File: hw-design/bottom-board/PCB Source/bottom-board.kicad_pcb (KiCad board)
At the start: 2 copper layers, 172 x 140.5 mm, 330 parts, among them J1 Power Jack, J10 NYS215, J11 USB_B, J12 USB_A, J13 DIN_5, J14 DIN_5, J15 RJHSE-5381, J16 NYS215, J17 NYS215, J18 MJ-3536N, J2 HMI_POWER, J3 CB Adapter, J4 CB Adapter, J5 HMI_DATA, J6 SERIAL_DEBUG, J7 NYS215, J8 NYS215, J9 NYS215, K1 G6S-2, K2 G6S-2, Q1 2N7002, Q10 J110, Q11 J110, Q12 2N7002, Q13 2N7002, Q14 J110, Q15 J110, Q16 2N7002, Q17 J110, Q2 2N7002, Q3 2N7002, Q4 2N7002, Q5 BSS84, Q6 BSS84, Q8 J110, Q9 2N7002, U1 MURATA 5V, U10 LM358, U11 OPA1678, U12 OPA1678, U13 DG9426E, U14 LM4811, U16 RT9742, U17 6N136S, U18 ISL83086E, U2 LD1117S50TR_SOT223, U20 ADC122S021, U21 MIC2076A, U22 74LVC3G17, U24 MCP4922-EP, U3 AP2120N-3.3, U4 LD1117S50TR_SOT223, U5 AP2120N-3.3, U6 CS4265, U7 AT24CS08, U8 LM4562, U9 DG9426E, X1 24.576MHz

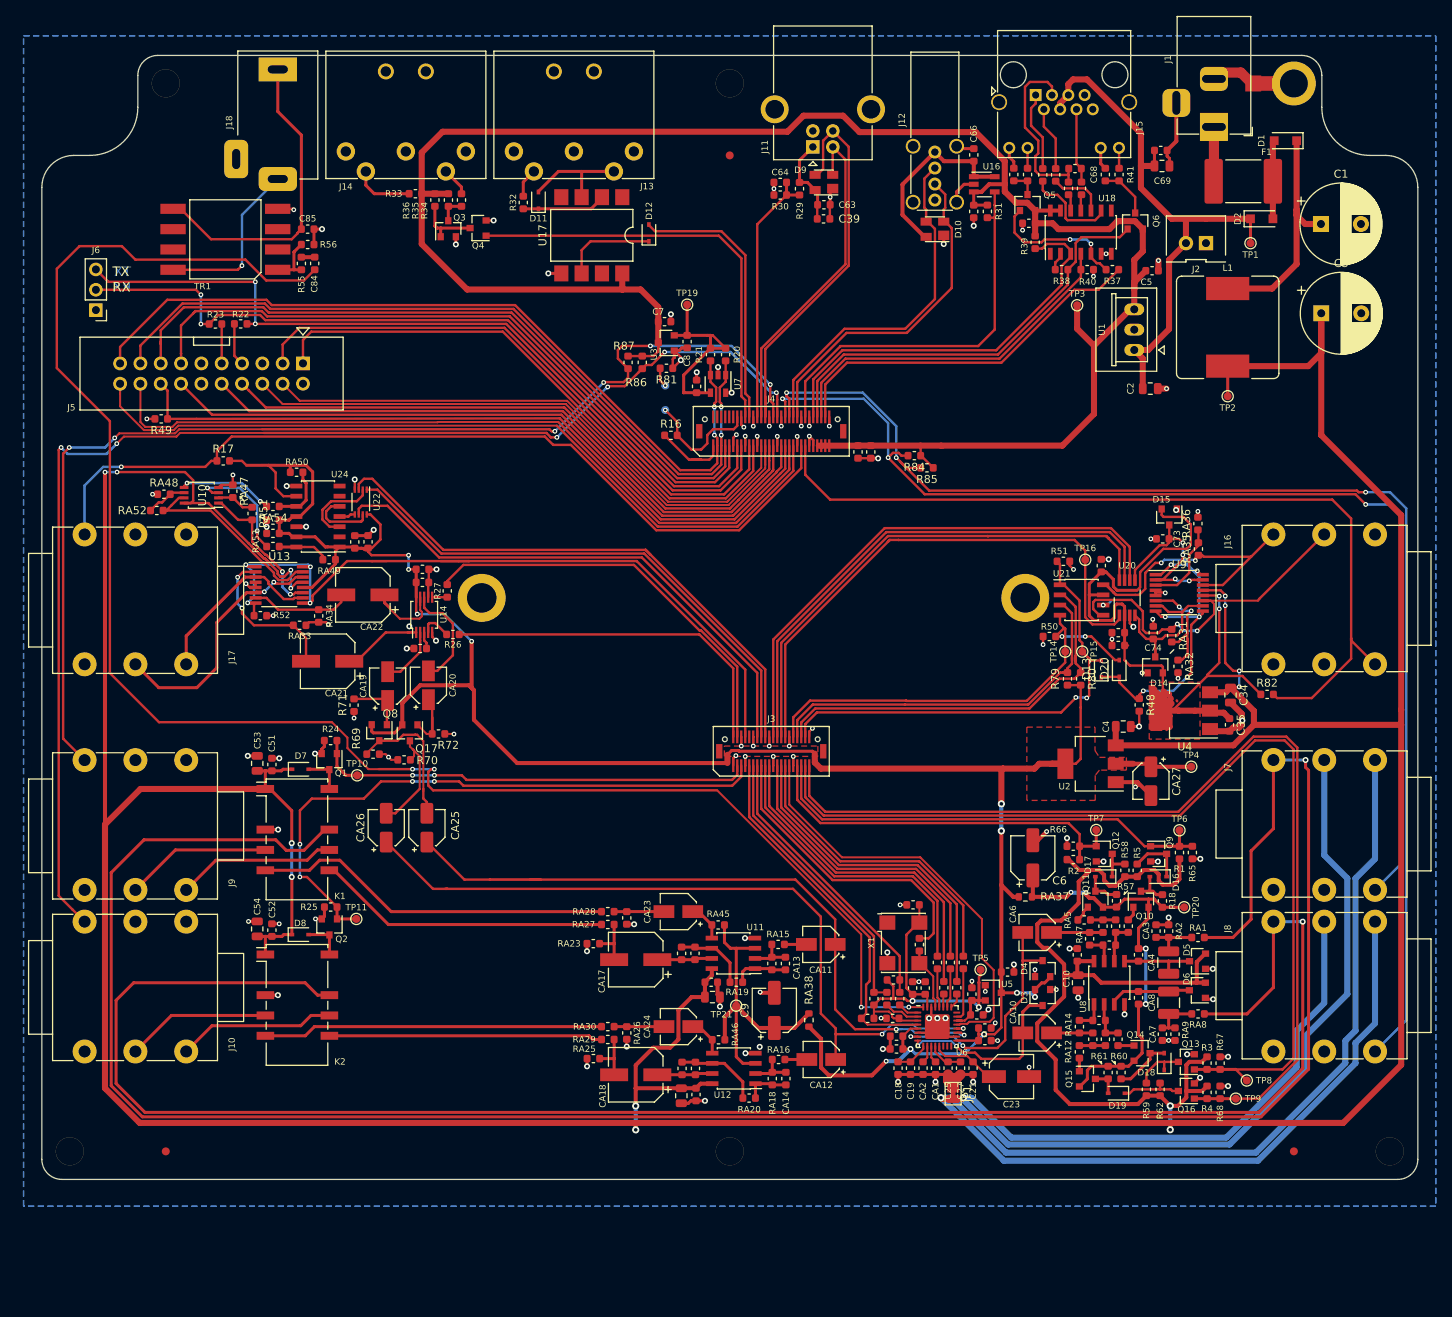
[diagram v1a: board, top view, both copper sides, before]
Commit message: route new output circuit
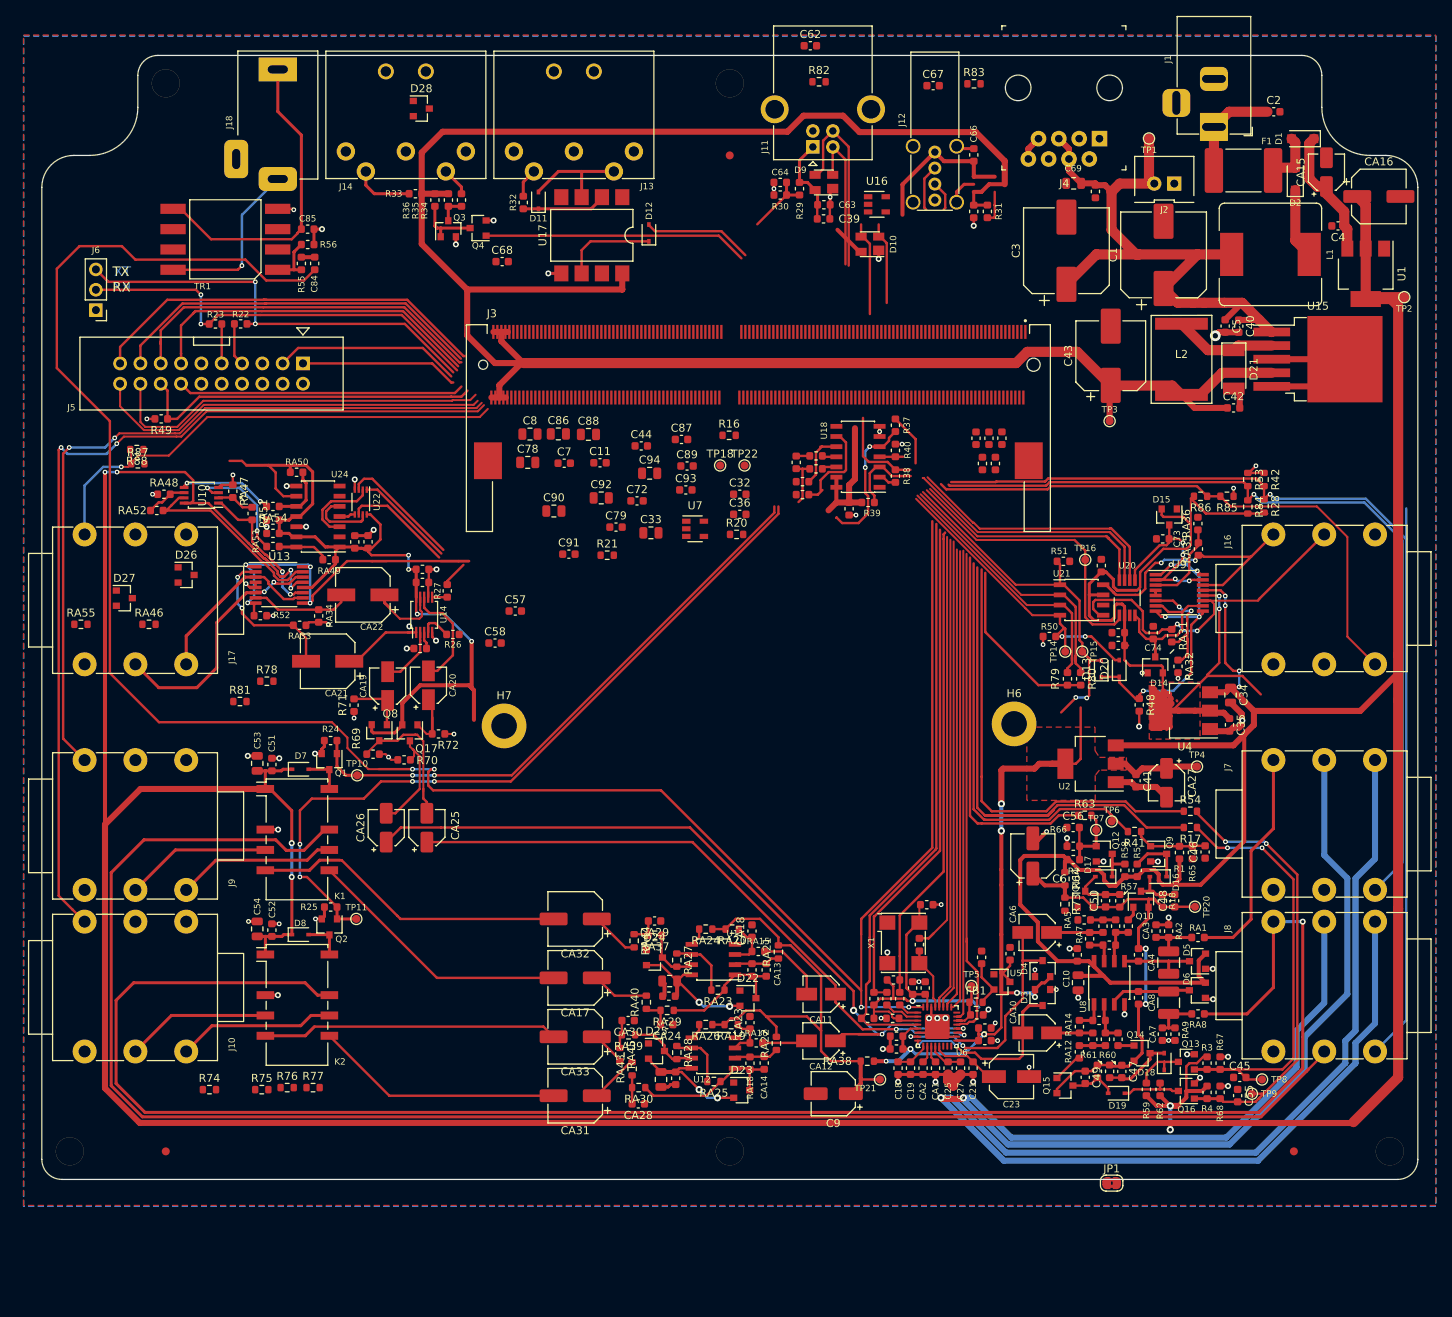
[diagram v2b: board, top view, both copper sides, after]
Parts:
- removed J15: RJHSE-5381, Connector_RJ:RJ45_Amphenol_RJHSE538X
- removed JMP1: 0R, footprints:Jumper_SMD_THT
- removed Q5, Q6: BSS84, Package_TO_SOT_SMD:SOT-23
- removed TP19: TestPoint, TestPoint:TestPoint_Pad_D1.0mm
- removed U3: AP2120N-3.3, Package_TO_SOT_SMD:SOT-23
- added C11: 100nF, Capacitor_SMD:C_0603_1608Metric, F.Cu at (129.8, 70.5)
- added C40: 100nF, Capacitor_SMD:C_0603_1608Metric, F.Cu at (209.7, 53.4)
- added C41: 100nF, Capacitor_SMD:C_0603_1608Metric, F.Cu at (196.8, 110.2)
- added C42: 100nF, Capacitor_SMD:C_0603_1608Metric, F.Cu at (209.0, 63.6)
- added C43: 470uF, Capacitor_SMD:CP_Elec_8x10.5, F.Cu at (193.7, 57.1)
- added C44: 1nF, Capacitor_SMD:C_0603_1608Metric, F.Cu at (135.0, 68.4)
- added C45: 100nF, Capacitor_SMD:C_0603_1608Metric, F.Cu at (209.8, 147.3)
- added C46: 100nF, Capacitor_SMD:C_0603_1608Metric, F.Cu at (205.5, 119.1)
- added C47: 100nF, Capacitor_SMD:C_0603_1608Metric, F.Cu at (195.1, 146.6)
- added C48: 100nF, Capacitor_SMD:C_0603_1608Metric, F.Cu at (201.7, 125.2)
- added C49: 100nF, Capacitor_SMD:C_0603_1608Metric, F.Cu at (190.5, 147.3)
- added C50: 100nF, Capacitor_SMD:C_0603_1608Metric, F.Cu at (193.0, 125.2)
- added C55: 100nF, Capacitor_SMD:C_0603_1608Metric, F.Cu at (209.6, 149.6)
- added C56: 100nF, Capacitor_SMD:C_0603_1608Metric, F.Cu at (189.0, 116.1)
- added C57: 100nF, Capacitor_SMD:C_0603_1608Metric, F.Cu at (119.3, 89.0)
- added C58: 100nF, Capacitor_SMD:C_0603_1608Metric, F.Cu at (116.7, 93.0)
- added C62: 1uF, Capacitor_SMD:C_0603_1608Metric, F.Cu at (156.1, 18.4)
- added C72: 100nF, Capacitor_SMD:C_0603_1608Metric, F.Cu at (134.5, 75.2)
- added C78: 22uF, Capacitor_SMD:C_0805_2012Metric, F.Cu at (120.8, 70.4)
- added C79: 100nF, Capacitor_SMD:C_0603_1608Metric, F.Cu at (131.8, 78.5)
- added C86: 22uF, Capacitor_SMD:C_0805_2012Metric, F.Cu at (124.6, 66.9)
- added C87: 100nF, Capacitor_SMD:C_0603_1608Metric, F.Cu at (140.0, 67.6)
- added C88: 22uF, Capacitor_SMD:C_0805_2012Metric, F.Cu at (128.4, 66.9)
- added C89: 100nF, Capacitor_SMD:C_0603_1608Metric, F.Cu at (140.7, 70.9)
- added C90: 22uF, Capacitor_SMD:C_0805_2012Metric, F.Cu at (124.1, 76.5)
- added C91: 100nF, Capacitor_SMD:C_0603_1608Metric, F.Cu at (126.0, 81.9)
- added C92: 22uF, Capacitor_SMD:C_0805_2012Metric, F.Cu at (130.0, 74.9)
- added C93: 100nF, Capacitor_SMD:C_0603_1608Metric, F.Cu at (140.6, 73.9)
- added C94: 22uF, Capacitor_SMD:C_0805_2012Metric, F.Cu at (136.1, 71.8)
- added CA28: 100pF, Capacitor_SMD:C_0603_1608Metric, F.Cu at (134.6, 150.6)
- added CA29: 100pF, Capacitor_SMD:C_0603_1608Metric, F.Cu at (136.7, 127.8)
- added CA30: 100pF, Capacitor_SMD:C_0603_1608Metric, F.Cu at (133.4, 140.2)
- added CA31: 47uF, Capacitor_SMD:CP_Elec_6.3x7.7, F.Cu at (126.7, 149.6)
- added CA32: 47uF, Capacitor_SMD:CP_Elec_6.3x7.7, F.Cu at (126.7, 127.5)
- added CA33: 47uF, Capacitor_SMD:CP_Elec_6.3x7.7, F.Cu at (126.7, 142.2)
- added D21: D_Schottky-Device, Diode_SMD:D_MELF, F.Cu at (209.1, 58.8)
- added D22: BAT54S, Package_TO_SOT_SMD:SOT-23, F.Cu at (148.3, 137.4)
- added D23: BAT54S, Package_TO_SOT_SMD:SOT-23, F.Cu at (147.6, 148.9)
- added D24: BAT54S, Package_TO_SOT_SMD:SOT-23, F.Cu at (136.7, 132.3)
- added D25: BAT54S, Package_TO_SOT_SMD:SOT-23, F.Cu at (136.9, 144.0)
- added D26: BAT54S, Package_TO_SOT_SMD:SOT-23, F.Cu at (78.1, 84.5)
- added D27: BAT54S, Package_TO_SOT_SMD:SOT-23, F.Cu at (70.4, 87.4)
- added D28: BAT54S, Package_TO_SOT_SMD:SOT-23, F.Cu at (107.5, 26.2)
- added FB1: Ferrite_Bead, Resistor_SMD:R_0603_1608Metric, F.Cu at (176.8, 137.9)
- added L2: 47UH 2A 135 MOHM, Uno:SRN8040TA, F.Cu at (202.5, 58.2)
- added R28: 100K, Resistor_SMD:R_0603_1608Metric, F.Cu at (212.9, 75.9)
- added R53: 56K, Resistor_SMD:R_0603_1608Metric, F.Cu at (210.8, 72.6)
- added R54: 1K, Resistor_SMD:R_0603_1608Metric, F.Cu at (203.6, 114.0)
- added R63: 1K, Resistor_SMD:R_0603_1608Metric, F.Cu at (190.4, 114.6)
- added R64: 1K, Resistor_SMD:R_0603_1608Metric, F.Cu at (188.0, 122.5)
- added R73: 1K5, Resistor_SMD:R_0603_1608Metric, F.Cu at (188.0, 125.7)
- added R74: 100K, Resistor_SMD:R_0603_1608Metric, F.Cu at (81.0, 148.8)
- added R75: 100K, Resistor_SMD:R_0603_1608Metric, F.Cu at (87.6, 148.8)
- added R76: 56K, Resistor_SMD:R_0603_1608Metric, F.Cu at (90.7, 148.6)
- added R77: 56K, Resistor_SMD:R_0603_1608Metric, F.Cu at (94.0, 148.6)
- added R78: 1M, Resistor_SMD:R_0603_1608Metric, F.Cu at (88.2, 97.8)
- added R83: 1M, Resistor_SMD:R_0603_1608Metric, F.Cu at (176.6, 23.1)
- added R88: 56K, Resistor_SMD:R_0603_1608Metric, F.Cu at (71.9, 68.8)
- added RA39: 150R, Resistor_SMD:R_0603_1608Metric, F.Cu at (133.4, 142.0)
- added RA40: 150R, Resistor_SMD:R_0603_1608Metric, F.Cu at (135.6, 137.9)
- added RA43: 150R, Resistor_SMD:R_0603_1608Metric, F.Cu at (133.9, 146.2)
- added RA44: 150R, Resistor_SMD:R_0603_1608Metric, F.Cu at (134.1, 130.2)
- added RA55: 6R8, Resistor_SMD:R_0603_1608Metric, F.Cu at (65.0, 90.7)
- added U15: LM2596S-5, Package_TO_SOT_SMD:TO-263-5_TabPin3, F.Cu at (219.6, 57.5)
- C1, C3: value 2200uF -> 1000uF; footprint Capacitor_THT:CP_Radial_D10.0mm_P5.00mm -> Capacitor_SMD:CP_Elec_10x10.5
- C2, C4: value 10uF 16V -> 100nF; footprint Capacitor_SMD:C_0805_2012Metric -> Capacitor_SMD:C_0603_1608Metric
- C33, C8: value 10uF -> 22uF; footprint Capacitor_SMD:C_0603_1608Metric -> Capacitor_SMD:C_0805_2012Metric
- C5: value 10uF -> 1nF
- C67: value 10uF -> 1uF
- C68: value 10uF -> 100nF
- C7: value 1uF -> 100nF
- CA15: value 100pF -> 10uF; footprint Capacitor_SMD:C_0603_1608Metric -> Capacitor_SMD:CP_Elec_4x5.7
- CA16: value 100pF -> 100uF; footprint Capacitor_SMD:C_0603_1608Metric -> Capacitor_SMD:CP_Elec_6.3x7.7
- CA17: value 100uF -> 47uF
- CA18: value 100uF -> 100pF; footprint Capacitor_SMD:CP_Elec_6.3x7.7 -> Capacitor_SMD:C_0603_1608Metric
- CA23, CA24: value 10uF -> 100pF; footprint Capacitor_SMD:CP_Elec_4x5.7 -> Capacitor_SMD:C_0603_1608Metric
- D1, D2: value MBR230 -> RSX205
- D13, D20: value 1N4148WS-Diode -> 1N4148
- H6, H7: footprint footprints:9774027151R -> MountingHole:MountingHole_3.2mm_M3_DIN965_Pad
- J3: value CB Adapter -> AS0A823-H4SB-7H; footprint footprints:DF12(3.0)-40DP-0.5V(86) -> Uno:TE_2309409-1
- J4: value CB Adapter -> RJ45; footprint footprints:DF12(3.0)-60DP-0.5V(86) -> digikey-footprints:Ethernet_Jack_54602-908LF
- JP1: footprint Jumper:SolderJumper-2_P1.3mm_Bridged_Pad1.0x1.5mm -> Jumper:SolderJumper-2_P1.3mm_Bridged2Bar_RoundedPad1.0x1.5mm
- R16: value 10K -> 10R
- R17: value 10K -> 1K
- R29: value 5K6 -> 10K
- R30: value 10K -> 15K
- R41: value 220R -> 1K
- R42: value 220R -> 56K
- R6, R7, R8: value 10K -> 2K7
- R81: value 10R -> 1M
- R82: value 10K -> 1M
- R84, R86, R87: value 10K -> 100K
- R85: value 10K -> 56K
- RA23, RA25: value 22K 1% -> 10K 1%
- RA24, RA26, RA28: value 33R -> 10K 1%
- RA27: value 66.5R 1% -> 10K 1%
- RA29: value 66.5R 1% -> 150R
- RA3: value 5K62 1% -> 5K6 1%
- RA30: value 33R -> 150R
- RA37: value 100R 1% -> 150R
- RA4: value 21K 1% -> 22K 1%
- RA45: value 10K 1% -> 150R
- RA46: value 10K 1% -> 6R8
- RA5, RA6: value 4K99 1% -> 4K7 1%
- TP18, TP22: moved to F.Cu
- U1: value MURATA 5V -> TL750M10CKVURG3; footprint footprints:OKI-78SR_Vertical -> Package_TO_SOT_SMD:SOT-223-3_TabPin2
- U16: value RT9742 -> TPS2041B; footprint Package_TO_SOT_SMD:TSOT-23-5 -> Package_TO_SOT_SMD:SOT-23-5
- U2: value LD1117S50TR_SOT223 -> LD1117S50TR
- moved CA16 138.5 mm to (227.2, 37.2), turned to 0 degrees
- moved R17 129.3 mm to (203.6, 116.1)
- moved CA15 125.6 mm to (220.7, 34.2)
- moved IMG1 124.4 mm to (273.3, 91.4)
- moved R82 94.9 mm to (157.2, 22.9)
- moved RA46 88.1 mm to (73.5, 90.7), turned to 0 degrees
- moved R41 82.1 mm to (196.7, 116.6), turned to 180 degrees
- moved C68 76.2 mm to (117.6, 45.3), turned to 0 degrees
- moved R86 71.8 mm to (204.9, 74.7), turned to 180 degrees
- moved C4 68.1 mm to (222.1, 40.9), turned to 180 degrees
- moved R81 67.7 mm to (84.8, 100.3), turned to 0 degrees
- moved R11 65.7 mm to (180.1, 67.4)
- moved R12 65.7 mm to (179.3, 70.6)
- moved R13 65.7 mm to (176.8, 67.4)
- moved R14 65.7 mm to (177.7, 70.6)
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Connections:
- C1 pad 1: Net-(C1-Pad1) -> +12V
- C1 pad 2: GND -> GNDD
- C10 pad 1: +12VA -> +10V
- C10 pad 2: GND -> GNDA
- C12 pad 1: GND -> GNDA
- C12 pad 2: +12VA -> +10V
- C13 pad 1: +12VA -> +10V
- C13 pad 2: GND -> GNDA
- C14 pad 1: GND -> GNDA
- C14 pad 2: +12VA -> +10V
- C15 pad 2: GND -> GNDA
- C16 pad 1: +3.3VA -> Net-(C16-Pad1)
- C16 pad 2: GND -> GNDA
- C17 pad 1: GND -> GNDA
- C18 pad 1: GND -> GNDA
- C19 pad 2: GND -> GNDA
- C2 pad 1: +12V -> Net-(C2-Pad1)
- C2 pad 2: GND -> GNDD
- C20 pad 1: GND -> GNDA
- C21 pad 1: GND -> GNDA
- C22 pad 1: GND -> GNDA
- C23 pad 2: GND -> GNDA
- C24 pad 1: GND -> GNDA
- C25 pad 1: GND -> GNDA
- C26 pad 2: GND -> GNDA
- C27 pad 2: GND -> GNDA
- C28 pad 1: GND -> GNDA
- C29 pad 2: GND -> GNDA
- C3 pad 1: +12VA -> +12V
- C3 pad 2: GND -> GNDD
- C30 pad 1: GND -> GNDA
- C31 pad 2: GND -> GNDA
- C32 pad 1: GND -> GNDD
- C33 pad 2: GND -> GNDD
- C34 pad 1: +12VA -> +10V
- C34 pad 2: GND -> GNDA
- C35 pad 2: GND -> GNDA
- C36 pad 2: GND -> GNDD
- C37 pad 1: GND -> GNDA
- C37 pad 2: +12VA -> +10V
- C38 pad 1: +12VA -> +10V
- C38 pad 2: GND -> GNDA
- C39 pad 1: GND -> GNDD
- C4 pad 1: +12VA -> Net-(C4-Pad1)
- C4 pad 2: GND -> GNDD
- C5 pad 1: +5VD -> +12V
- C5 pad 2: GND -> GNDD
- C51 pad 1: GND -> GNDA
- C51 pad 2: +12VA -> +10V
- C52 pad 1: GND -> GNDA
- C52 pad 2: +12VA -> +10V
- C53 pad 1: +12VA -> +10V
- C53 pad 2: GND -> GNDA
- C54 pad 1: +12VA -> +10V
- C54 pad 2: GND -> GNDA
- C59 pad 2: GND -> GNDA
- C6 pad 2: GND -> GNDA
- C60 pad 1: GND -> GNDA
- C61 pad 2: GND -> GNDA
- C63 pad 2: GND -> GNDD
- C64 pad 2: GND -> GNDD
- C65 pad 2: GND -> GNDD
- C66 pad 1: GND -> GNDD
- C67 pad 1: RS485_TX_LED -> Net-(C67-Pad1)
- C67 pad 2: GND -> GNDD
- C68 pad 1: RS485_RX_LED -> GNDD
- C68 pad 2: GND -> +5VD
- C69 pad 2: GND -> GNDD
- C7 pad 1: +5VD -> GNDD
- C7 pad 2: GND -> +3V0
- C70 pad 2: GND -> GNDD
- C71 pad 2: GND -> GNDD
- C73 pad 2: GND -> GNDA
- C74 pad 2: GND -> GNDA
- C75 pad 1: GND -> GNDA
- C76 pad 2: GND -> GNDA
- C77 pad 1: GND -> GNDA
- C8 pad 1: +3V3 -> +3V0
- C8 pad 2: GND -> GNDD
- C80 pad 1: GND -> GNDA
- C81 pad 2: GND -> GNDA
- C82 pad 1: GND -> GNDA
- C83 pad 1: GND -> GNDA
- C85 pad 1: GND -> GNDD
- C9 pad 2: GND -> GNDA
- CA1 pad 2: GND -> GNDA
- CA15 pad 1: Net-(CA15-Pad1) -> Net-(C4-Pad1)
- CA15 pad 2: Net-(CA15-Pad2) -> GNDD
- CA16 pad 1: Net-(CA16-Pad1) -> +10V
- CA16 pad 2: Net-(CA16-Pad2) -> GNDA
- CA17 pad 1: Net-(CA15-Pad1) -> Net-(CA17-Pad1)
- CA18 pad 1: Net-(CA16-Pad1) -> Net-(CA18-Pad1)
- CA18 pad 2: Net-(CA18-Pad2) -> GNDA
- CA2 pad 2: GND -> GNDA
- CA21 pad 2: HP_LEFT -> Net-(CA21-Pad2)
- CA22 pad 2: HP_RIGHT -> Net-(CA22-Pad2)
- CA23 pad 2: Net-(CA23-Pad2) -> GNDA
- CA24 pad 1: Net-(CA24-Pad1) -> GNDA
- CA27 pad 2: GND -> GNDA
- CA3 pad 1: GND -> GNDA
- CA7 pad 1: GND -> GNDA
- D1 pad 1: Net-(C1-Pad1) -> Net-(C4-Pad1)
- D10 pad 1: GND -> GNDD
- D14 pad 1: GND -> GNDA
- D15 pad 1: GND -> GNDA
- D2 pad 1: +12V -> Net-(D2-Pad1)
- D3 pad 1: GND -> GNDA
- D4 pad 1: GND -> GNDA
- D5 pad 1: GND -> GNDA
- D5 pad 2: +12VA -> +10V
- D6 pad 1: GND -> GNDA
- D6 pad 2: +12VA -> +10V
- D7 pad 1: +12VA -> +10V
- D8 pad 1: +12VA -> +10V
- D9 pad 1: GND -> GNDD
- F1 pad 2: Net-(F1-Pad2) -> Net-(C2-Pad1)
- J1 pad 1: Net-(F1-Pad2) -> Net-(C2-Pad1)
- J1 pad 2: GND -> GNDD
- J1 pad 3: GND -> GNDD
- J10 pad S: GND -> GNDA
- J11 pad 4: GND -> GNDD
- J11 pad 5: GND -> Net-(C62-Pad1)
- J12 pad 4: GND -> GNDD
- J12 pad 5: GND -> Net-(C67-Pad1)
- J14 pad 2: GND -> GNDD
- J16 pad S: GND -> GNDA
- J17 pad S: GND -> GNDA
- J2 pad 1: GND -> GNDD
- J3 pad 1: GND -> GNDD
- J3 pad 10: (no net) -> CODEC_I2S_SDIN
- J3 pad 11: CODEC_I2C_SCL -> (no net)
- J3 pad 12: GND -> CODEC_I2S_SDOUT
- J3 pad 13: CODEC_I2C_SDA -> (no net)
- J3 pad 14: CV_DAC_~CS~ -> (no net)
- J3 pad 15: CODEC_I2S_MCLK -> (no net)
- J3 pad 16: CV_DAC_SDI -> (no net)
- J3 pad 17: CODEC_I2S_LRCK -> (no net)
- J3 pad 18: CV_DAC_SCK -> CODEC_SPDIF_SDIN
- J3 pad 19: CODEC_I2S_BCLK -> (no net)
- J3 pad 2: HP_CLOCK -> GNDD
- J3 pad 20: GND -> CODEC_I2S_MCLK
- J3 pad 21: GND -> (no net)
- J3 pad 22: CV_ADC_DIN -> CODEC_I2C_SDA
- J3 pad 23: CODEC_I2S_SDOUT -> (no net)
- J3 pad 24: CV_ADC_DOUT -> CODEC_I2C_SCL
- J3 pad 25: CODEC_I2S_SDIN -> (no net)
- J3 pad 26: CV_ADC_SCLK -> GNDD
- J3 pad 27: CODEC_SPDIF_SDIN -> (no net)
- J3 pad 28: CV_ADC_~CS~ -> CODEC_RESET
- J3 pad 29: CODEC_MUTEC -> (no net)
- J3 pad 3: IN1_TBP -> (no net)
- J3 pad 30: GND -> CODEC_MUTEC
- J3 pad 31: GND -> (no net)
- J3 pad 32: EXP_EN2 -> IN1_DETECT
- J3 pad 33: IN1_GC2 -> (no net)
- J3 pad 34: EXP_FLAG2 -> IN2_DETECT
- J3 pad 35: IN1_GC1 -> (no net)
- J3 pad 36: EXP_FLAG1 -> CV_IN_DET
- J3 pad 37: IN2_GC1 -> (no net)
- J3 pad 38: EXP_EN1 -> (no net)
- J3 pad 39: IN2_GC2 -> (no net)
- J3 pad 4: HP_UP/DN -> CODEC_I2S_BCLK
- J3 pad 40: GND -> GNDD
- J3 pad 5: IN2_TBP -> (no net)
- J3 pad 6: GND -> (no net)
- J3 pad 7: GND -> (no net)
- J3 pad 8: HP_DISABLE -> CODEC_I2S_LRCK
- J3 pad 9: CODEC_RESET -> (no net)
- J4 pad 1: VCC_SYS_1V8 -> RS485_TX+
- J4 pad 2: (no net) -> RS485_TX-
- J4 pad 3: PM_LEDS_SDA -> RS485_RX+
- J4 pad 4: (no net) -> +12V
- J4 pad 5: PM_LEDS_SCL -> +12V
- J4 pad 6: (no net) -> RS485_RX-
- J4 pad 7: PM_LEDS_OE -> GNDD
- J4 pad 8: (no net) -> GNDD
- J5 pad 10: HMI_SPI0_CS0 -> (no net)
- J5 pad 11: GND -> GNDD
- J5 pad 12: GND -> GNDD
- J5 pad 2: GND -> GNDD
- J5 pad 4: HMI_SPI0_MISO -> (no net)
- J5 pad 5: GND -> GNDD
- J5 pad 6: HMI_SPI0_MOSI -> (no net)
- J5 pad 8: HMI_SPI0_CLK -> (no net)
- J6 pad 1: GND -> GNDD
- J7 pad R: GNDS -> GNDA
- J7 pad S: GNDS -> GNDA
- J7 pad T: IN1 -> Net-(J7-PadT)
- J7 pad TN: GND -> GNDA
- J8 pad R: GNDS -> GNDA
- J8 pad S: GNDS -> GNDA
- J8 pad T: IN2 -> Net-(J8-PadT)
- J8 pad TN: GND -> GNDA
- J9 pad S: GND -> GNDA
- JP1 pad 1: GND -> GNDA
- JP1 pad 2: GNDS -> GNDD
- K1 pad 1: +12VA -> +10V
- K1 pad 10: IN1 -> (no net)
- K1 pad 3: GND -> GNDA
- K1 pad 5: Net-(K1-Pad5) -> Net-(CA32-Pad2)
- K1 pad 8: Net-(K1-Pad8) -> Net-(CA17-Pad2)
- K2 pad 1: +12VA -> +10V
- K2 pad 10: IN2 -> (no net)
- K2 pad 3: GND -> GNDA
- K2 pad 5: Net-(K2-Pad5) -> Net-(CA33-Pad2)
- K2 pad 8: Net-(K2-Pad8) -> Net-(CA31-Pad2)
- L1 pad 1: Net-(C1-Pad1) -> Net-(D2-Pad1)
- L1 pad 2: +12VA -> +12V
- Q1 pad 2: GND -> GNDA
- Q12 pad 1: IN1_GC2 -> Net-(C56-Pad2)
- Q12 pad 2: GND -> GNDA
- Q13 pad 1: IN2_GC1 -> Net-(C45-Pad2)
- Q13 pad 2: GND -> GNDA
- Q16 pad 1: IN2_GC2 -> Net-(C55-Pad2)
- Q16 pad 2: GND -> GNDA
- Q2 pad 2: GND -> GNDA
- Q3 pad 2: GND -> GNDD
- Q4 pad 2: GND -> GNDD
- Q9 pad 1: IN1_GC1 -> Net-(C46-Pad2)
- Q9 pad 2: GND -> GNDA
- R1 pad 1: +12VA -> +10V
- R1 pad 2: IN1_GC1 -> Net-(C46-Pad2)
- R16 pad 1: VCC_SYS_1V8 -> UBOOT_BUTTON
- R16 pad 2: UBOOT_BUTTON -> Net-(R16-Pad2)
- R17 pad 1: +5VA -> Net-(C45-Pad2)
- R17 pad 2: CV_OUT_DET -> IN2_GC1
- R2 pad 1: +12VA -> +10V
- R2 pad 2: IN1_GC2 -> Net-(C56-Pad2)
- R24 pad 2: GND -> GNDA
- R25 pad 2: GND -> GNDA
- R3 pad 1: +12VA -> +10V
- R3 pad 2: IN2_GC1 -> Net-(C45-Pad2)
- R30 pad 2: GND -> GNDD
- R31 pad 1: USB_HOST_DRV -> GNDD
- R31 pad 2: +5VD -> USB_HOST_DRV
- R4 pad 1: +12VA -> +10V
- R4 pad 2: IN2_GC2 -> Net-(C55-Pad2)
- R40 pad 2: GND -> GNDD
- R41 pad 1: Net-(J15-Pad12) -> Net-(C46-Pad2)
- R41 pad 2: RS485_RX_LED -> IN1_GC1
- R42 pad 1: Net-(J15-Pad10) -> GNDD
- R42 pad 2: RS485_TX_LED -> IN2_DETECT
- R48 pad 2: GND -> GNDA
- R49 pad 2: GND -> GNDD
- R5 pad 1: +12VA -> +10V
- R50 pad 2: GND -> GNDA
- R51 pad 2: GND -> GNDA
- R52 pad 2: GND -> GNDA
- R56 pad 2: GND -> GNDD
- R58 pad 1: +12VA -> +10V
- R59 pad 1: +12VA -> +10V
- R62 pad 1: +12VA -> +10V
- R65 pad 1: GND -> GNDA
- R65 pad 2: IN1_GC1 -> Net-(C46-Pad2)
- R66 pad 1: GND -> GNDA
- R66 pad 2: IN1_GC2 -> Net-(C56-Pad2)
- R67 pad 1: GND -> GNDA
- R67 pad 2: IN2_GC1 -> Net-(C45-Pad2)
- R68 pad 1: GND -> GNDA
- R68 pad 2: IN2_GC2 -> Net-(C55-Pad2)
- R69 pad 1: GND -> GNDA
- R70 pad 1: GND -> GNDA
- R71 pad 1: GND -> GNDA
- R72 pad 1: GND -> GNDA
- R79 pad 2: +5VA -> +3V0
- R80 pad 2: +5VA -> +3V0
- R81 pad 1: GND -> Net-(CA26-Pad2)
- R81 pad 2: Net-(R81-Pad2) -> +5VA
- R82 pad 1: +5VP -> GNDD
- R82 pad 2: CV_IN_DET -> Net-(C62-Pad1)
- R84 pad 1: +5VD -> IN1_DETECT
- R84 pad 2: IN1_DETECT -> +5VP
- R85 pad 1: +5VD -> GNDD
- R85 pad 2: IN2_DETECT -> CV_IN_DET
- R86 pad 1: +5VD -> CV_IN_DET
- R86 pad 2: OUT2_DETECT -> +5VP
- R87 pad 1: +5VD -> CV_OUT_DET
- R87 pad 2: OUT1_DETECT -> +5VP
- RA1 pad 2: IN1 -> Net-(J7-PadT)
- RA15 pad 2: Net-(CA13-Pad2) -> Net-(CA18-Pad1)
- RA16 pad 2: Net-(CA14-Pad2) -> Net-(CA23-Pad1)
- RA19 pad 1: Net-(CA13-Pad1) -> Net-(CA23-Pad1)
- RA19 pad 2: Net-(CA15-Pad2) -> /audio-outputs/OUTPUT_BIAS
- RA2 pad 1: GND -> GNDA
- RA20 pad 1: Net-(CA14-Pad1) -> Net-(CA18-Pad1)
- RA20 pad 2: Net-(CA16-Pad2) -> /audio-outputs/OUTPUT_BIAS
- RA21 pad 1: Net-(CA15-Pad2) -> Net-(CA13-Pad2)
- RA21 pad 2: Net-(CA15-Pad1) -> /audio-outputs/OUTPUT_BIAS
- RA22 pad 1: Net-(CA16-Pad2) -> Net-(CA14-Pad2)
- RA22 pad 2: Net-(CA16-Pad1) -> /audio-outputs/OUTPUT_BIAS
- RA23 pad 1: Net-(CA17-Pad2) -> Net-(CA13-Pad1)
- RA23 pad 2: GND -> Net-(RA23-Pad2)
- RA24 pad 1: GND -> /audio-outputs/OUTPUT_BIAS
- RA24 pad 2: Net-(CA23-Pad2) -> Net-(RA24-Pad2)
- RA25 pad 1: Net-(CA18-Pad2) -> Net-(CA14-Pad1)
- RA25 pad 2: GND -> Net-(RA25-Pad2)
- RA26 pad 1: GND -> /audio-outputs/OUTPUT_BIAS
- RA26 pad 2: Net-(CA24-Pad2) -> Net-(RA26-Pad2)
- RA27 pad 1: Net-(K1-Pad8) -> Net-(RA23-Pad2)
- RA27 pad 2: Net-(CA17-Pad2) -> Net-(D24-Pad3)
- RA28 pad 1: Net-(K1-Pad5) -> Net-(RA25-Pad2)
- RA28 pad 2: Net-(CA23-Pad2) -> Net-(D25-Pad3)
- RA29 pad 1: Net-(K2-Pad8) -> Net-(CA13-Pad1)
- RA29 pad 2: Net-(CA18-Pad2) -> Net-(CA24-Pad2)
- RA30 pad 1: Net-(K2-Pad5) -> Net-(CA14-Pad1)
- RA30 pad 2: Net-(CA24-Pad2) -> Net-(CA28-Pad2)
- RA32 pad 2: GND -> GNDA
- RA33 pad 1: HP_LEFT -> Net-(CA21-Pad2)
- RA33 pad 2: GND -> GNDA
- RA34 pad 1: HP_RIGHT -> Net-(CA22-Pad2)
- RA34 pad 2: GND -> GNDA
- RA36 pad 2: GND -> GNDA
- RA37 pad 1: +5VA -> Net-(D24-Pad3)
- RA37 pad 2: /audio-inputs/INPUT_BIAS -> Net-(CA29-Pad2)
- RA45 pad 1: /audio-outputs/OUTPUT_BIAS -> Net-(CA30-Pad2)
- RA45 pad 2: Net-(CA23-Pad1) -> Net-(CA33-Pad1)
- RA46 pad 1: /audio-outputs/OUTPUT_BIAS -> Net-(CA21-Pad2)
- RA46 pad 2: Net-(CA24-Pad1) -> HP_LEFT
- RA47 pad 1: GND -> GNDA
- RA48 pad 1: GND -> GNDA
- RA8 pad 2: IN2 -> Net-(J8-PadT)
- RA9 pad 1: GND -> GNDA
- TP18 pad 1: Net-(R81-Pad2) -> GNDD
- TP2 pad 1: +12VA -> +10V
- TP22 pad 1: UBOOT_BUTTON -> Net-(R16-Pad2)
- TP7 pad 1: IN1_GC2 -> Net-(C56-Pad2)
- TP8 pad 1: IN2_GC1 -> Net-(C45-Pad2)
- TP9 pad 1: IN2_GC2 -> Net-(C55-Pad2)
- TR1 pad 4: GND -> GNDD
- U1 pad 1: +12V -> GNDA
- U1 pad 2: GND -> +10V
- U1 pad 3: +5VD -> Net-(C4-Pad1)
- U10 pad 4: GND -> GNDA
- U10 pad 8: +12VA -> +10V
- U11 pad 3: /audio-outputs/OUTPUT_BIAS -> Net-(CA18-Pad1)
- U11 pad 4: GND -> GNDA
- U11 pad 5: Net-(CA23-Pad1) -> Net-(RA24-Pad2)
- U11 pad 6: Net-(CA15-Pad2) -> Net-(RA23-Pad2)
- U11 pad 7: Net-(CA15-Pad1) -> Net-(D24-Pad3)
- U11 pad 8: +12VA -> +10V
- U12 pad 3: /audio-outputs/OUTPUT_BIAS -> Net-(CA23-Pad1)
- U12 pad 4: GND -> GNDA
- U12 pad 5: Net-(CA24-Pad1) -> Net-(RA26-Pad2)
- U12 pad 6: Net-(CA16-Pad2) -> Net-(RA25-Pad2)
- U12 pad 7: Net-(CA16-Pad1) -> Net-(D25-Pad3)
- U12 pad 8: +12VA -> +10V
- U13 pad 13: +12VA -> +10V
- U13 pad 4: GND -> GNDA
- U13 pad 5: GND -> GNDA
- U14 pad 5: GND -> GNDA
- U14 pad 7: GND -> GNDA
- U16 pad 2: GND -> GNDD
- U16 pad 3: +5VD -> (no net)
- U16 pad 5: Net-(C66-Pad2) -> +5VD
- U17 pad 5: GND -> GNDD
- U18 pad 6: GND -> GNDD
- U18 pad 7: GND -> GNDD
- U2 pad 1: GND -> GNDA
- U2 pad 3: +12VA -> +10V
- U20 pad 3: GND -> GNDA
- U21 pad 6: GND -> GNDA
- U22 pad 1: CV_DAC_SDI -> CV_ADC_DIN
- U22 pad 3: CV_DAC_SCK -> CV_ADC_SCLK
- U22 pad 4: GND -> (no net)
- U24 pad 12: GND -> GNDA
- U24 pad 8: GND -> GNDA
- U4 pad 1: GND -> GNDA
- U4 pad 3: +12VA -> +10V
- U5 pad 1: GND -> GNDA
- U5 pad 2: +3.3VA -> Net-(C16-Pad1)
- U6 pad 18: GND -> GNDA
- U6 pad 30: GND -> GNDA
- U6 pad 33: GND -> GNDA
- U6 pad 6: GND -> GNDA
- U7 pad 2: GND -> GNDD
- U7 pad 5: GND -> GNDD
- U8 pad 4: GND -> GNDA
- U8 pad 8: +12VA -> +10V
- U9 pad 13: +12VA -> +10V
- U9 pad 4: GND -> GNDA
- U9 pad 5: GND -> GNDA
- X1 pad 2: GND -> GNDA
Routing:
- net +10V: track 0.00 -> 680.2 mm, vias 0 -> 16
- net +12VA: track 675.5 -> 0.00 mm, vias 14 -> 0
- net GNDA: track 0.00 -> 455.9 mm, vias 0 -> 62
- net GNDS: track 337.4 -> 0.00 mm, vias 2 -> 0
- net IN1: track 282.2 -> 0.00 mm, vias 1 -> 0
- net GND: track 234.5 -> 2.27 mm, vias 130 -> 1
- net Net-(J8-PadT): track 0.00 -> 231.0 mm, vias 0 -> 1
- net IN2: track 231.0 -> 0.00 mm, vias 1 -> 0
- net (no net): track 0.01 -> 216.3 mm, vias 0 -> 1
- net +5VA: track 305.8 -> 217.2 mm
- net HMI_SPI0_CS0: track 80.8 -> 0.00 mm
- net HMI_SPI0_CLK: track 77.3 -> 0.00 mm
- net HMI_SPI0_MOSI: track 73.9 -> 0.00 mm
- net CV_DAC_SCK: track 70.9 -> 0.00 mm
- net HMI_SPI0_MISO: track 70.5 -> 0.00 mm
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- added copper zone on +5VD, net +5VD
- added copper zone on B.Cu, net GNDD
- added copper zone on F.Cu, net GNDD
- added copper zone on GNDD, net GNDD
- removed copper zone on B.Cu, net GND
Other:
- copper layers 2 -> 4
- board text removed: "PIN1"
- board text removed: "PIN40"
- board text removed: "PIN60"
- board text removed: "Recovery pads"

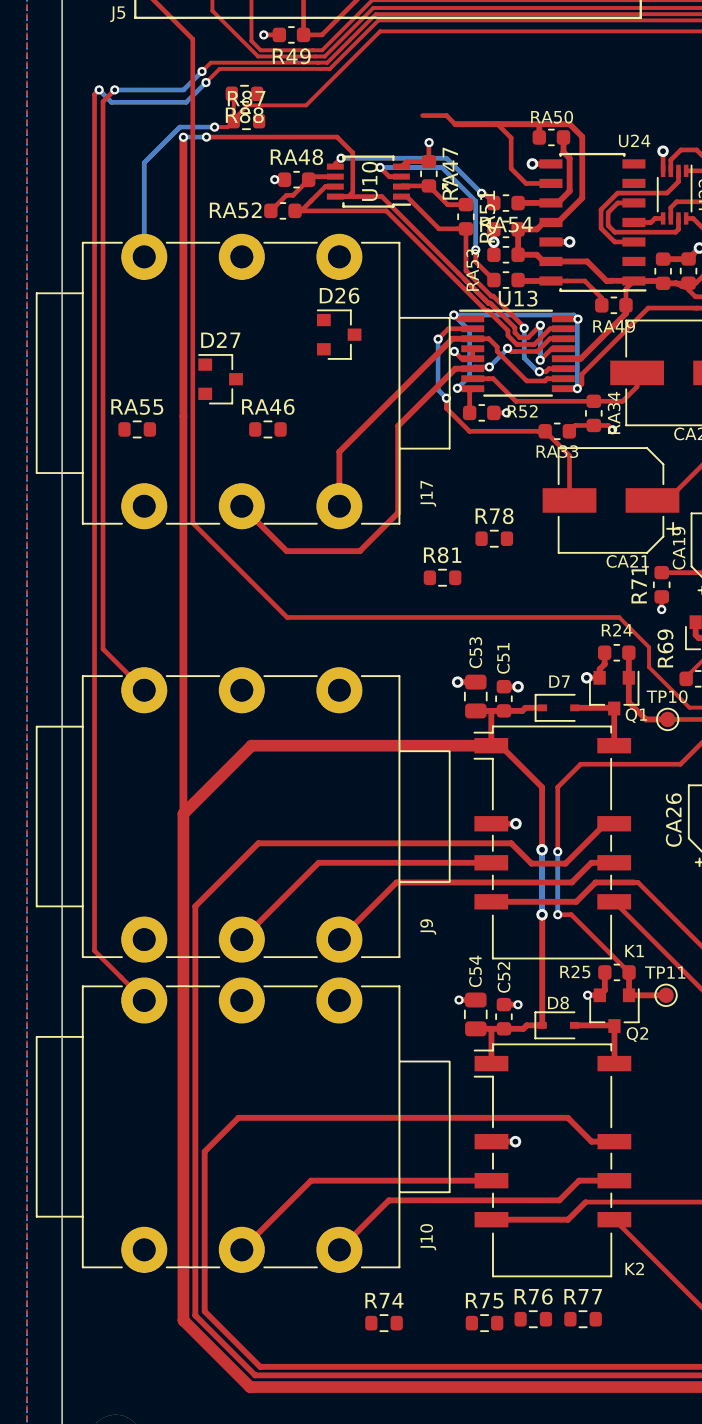
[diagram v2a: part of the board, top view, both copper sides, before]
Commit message: route output detect to GNDD
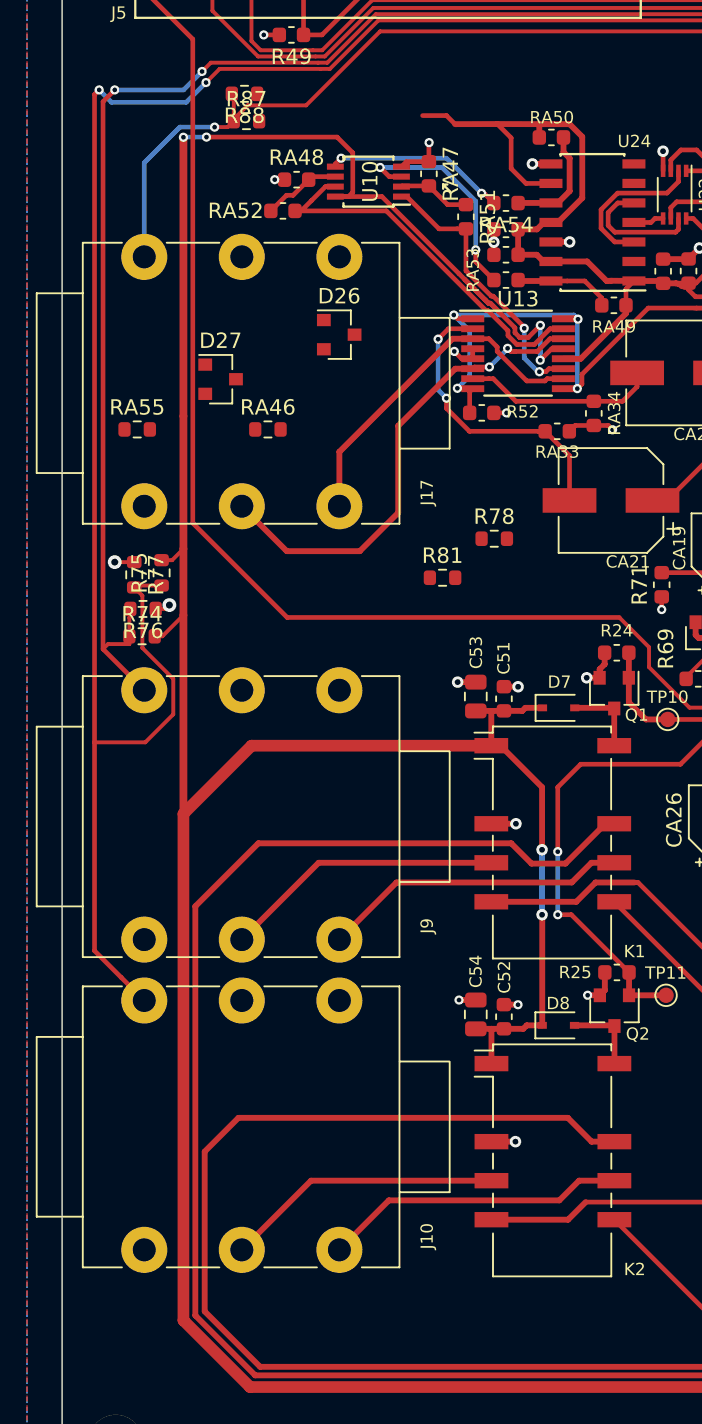
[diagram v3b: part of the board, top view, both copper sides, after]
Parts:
- R74, R75, R87: value 100K -> 220K
- R76, R77, R88: value 56K -> 47K
- moved R77 56.6 mm to (64.8, 100.1), turned to 270 degrees
- moved R75 53.2 mm to (66.5, 100.0), turned to 90 degrees
- moved R76 52.7 mm to (65.3, 102.4), turned to 180 degrees
- moved R74 47.4 mm to (65.3, 104.1)
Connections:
- R74 pad 2: +5VD -> +10V
- R75 pad 2: +5VD -> +10V
- R76 pad 1: GNDA -> GNDD
- R77 pad 1: GNDA -> GNDD
- R87 pad 2: +5VP -> +10V
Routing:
- net OUT2_DETECT: track 116.5 -> 133.7 mm
- net +10V: track 680.2 -> 684.4 mm
- net OUT1_DETECT: track 94.4 -> 98.0 mm
- net GNDD: track 59.0 -> 61.3 mm, vias 16 -> 18
